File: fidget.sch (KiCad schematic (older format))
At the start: 86 parts, among them J1 KEYSTONE 120, J2 KEYSTONE 120, U1 MCP73831-2ACI/MC, U2 ESP8285, U3 TLV70033DSE, U4 LIS2DE, U5 TPS60150, U6 TPS60150, U7 TPS60150, U8 TLV4946-2K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

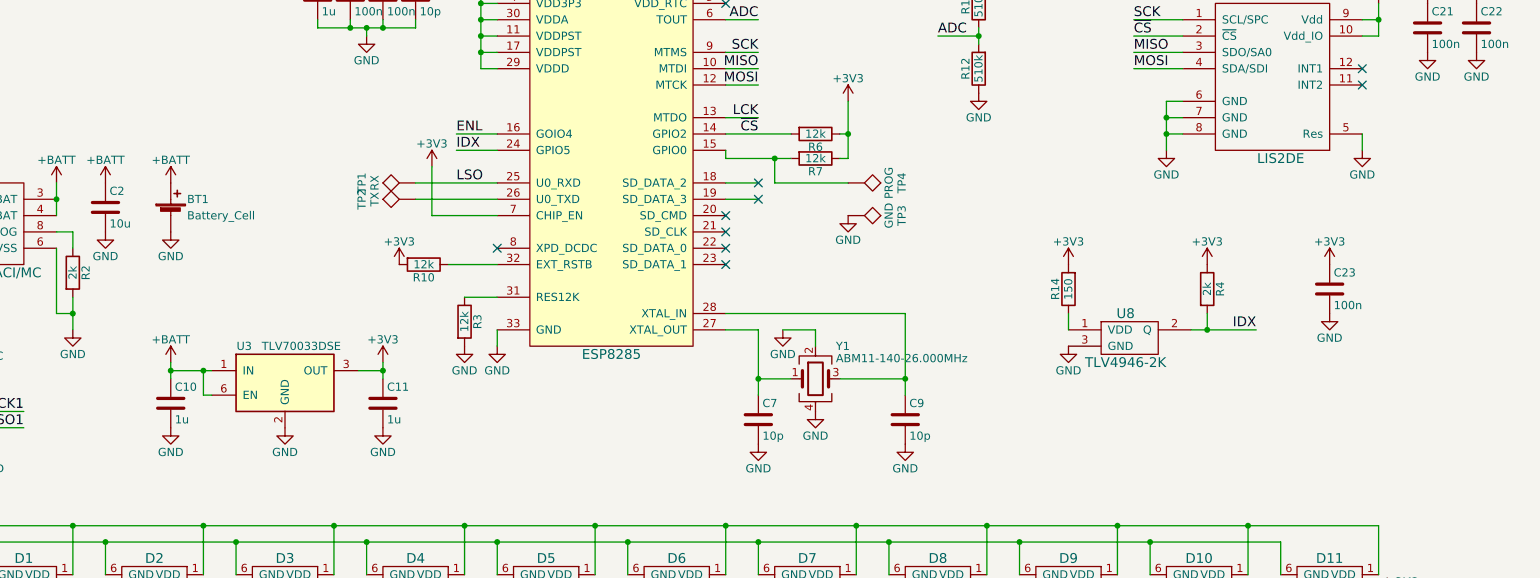
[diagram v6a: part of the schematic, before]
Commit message: added SLG46140 for UVLO and power management
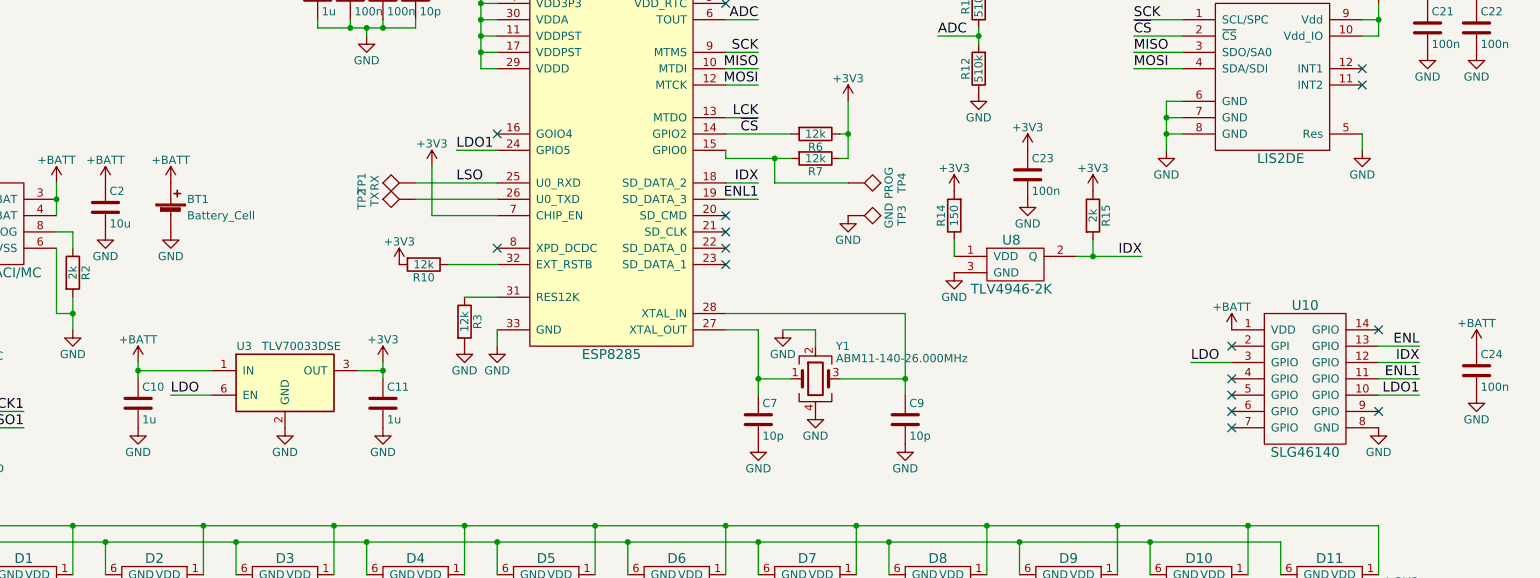
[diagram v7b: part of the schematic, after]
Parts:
- added C24: 100n, Capacitors_SMD:C_0402, symbol C
- added U10: SLG46140, parts:SILEGO_STQFN-14L-1.6x2mm_Pitch0.4mm, symbol SLG46140
- renumbered R4 to R15
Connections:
- net +BATT: now also C24.1, U10.1 (VDD); no longer U3.6 (EN)
- net ENL: now also U10.13 (GPIO); no longer U2.16 (GOIO4)
- net GND: now also C24.2, U10.8 (GND)
- net IDX: now also U2.18 (SD_DATA_2), U10.12 (GPIO); no longer U2.24 (GPIO5)
- net ENL1: now reaches U2.19 (SD_DATA_3)
- net ENL1: now also U10.11 (GPIO)
- new net LDO: U10.3 (GPIO), U3.6 (EN)
- new net LDO1: U10.10 (GPIO), U2.24 (GPIO5)
- no-connect marks 13 -> 19
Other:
- moved on the sheet: C10, C23, R14, R15, U8
